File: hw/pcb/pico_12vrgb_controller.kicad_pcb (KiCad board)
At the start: 2 copper layers, 101 x 31.8 mm, 20 parts, among them J1 Conn_01x04_RGB, J2 Conn_01x04_RGB, J3 Conn_01x04_RGB, J4 Conn_01x04_RGB, J5 Sata_15pin_Power, Q1 DMG2302U, Q10 DMG2302U, Q11 DMG2302U, Q12 DMG2302U, Q2 DMG2302U, Q3 DMG2302U, Q4 DMG2302U, Q5 DMG2302U, Q6 DMG2302U, Q7 DMG2302U, Q8 DMG2302U, Q9 DMG2302U, U1 Raspberry_Pi_Pico, U2 LM4040C30FTA

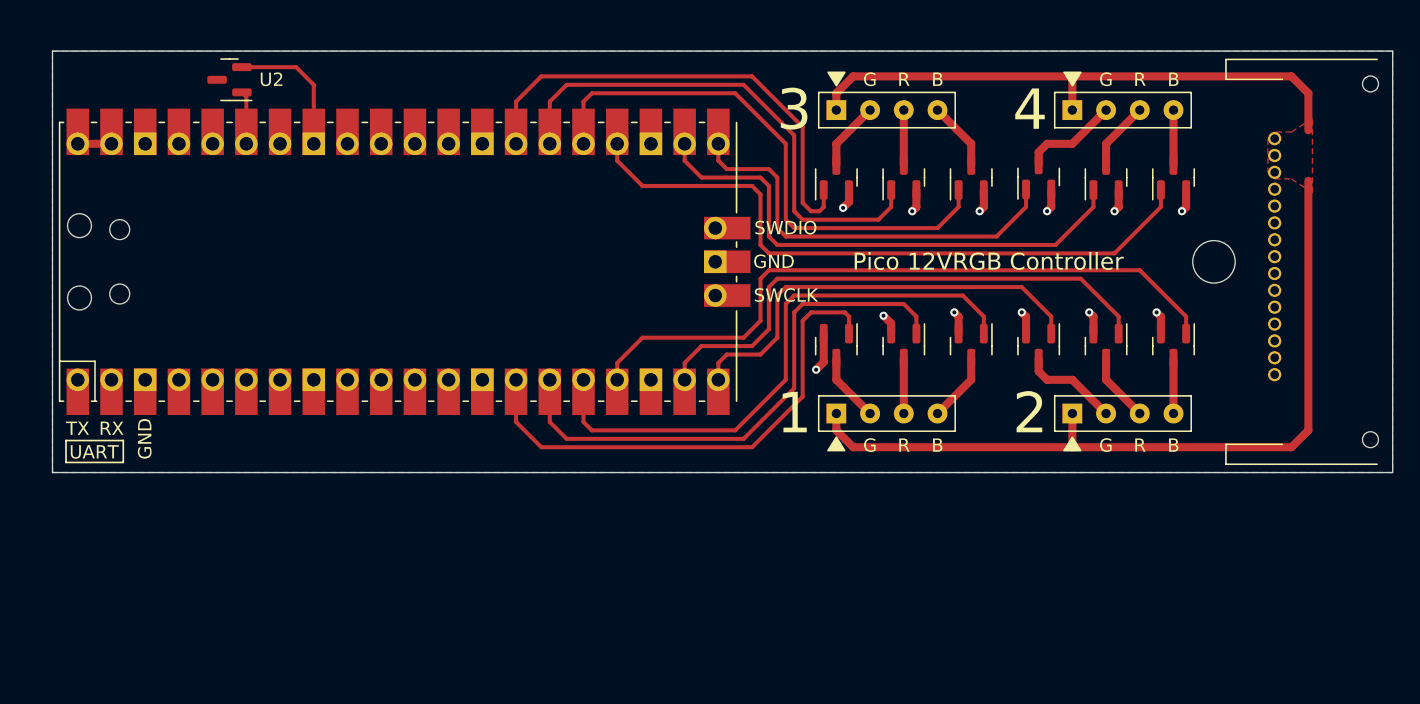
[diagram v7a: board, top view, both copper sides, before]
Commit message: Add missing silkscreen markings
Change debug label, add transistor markings, add version number.
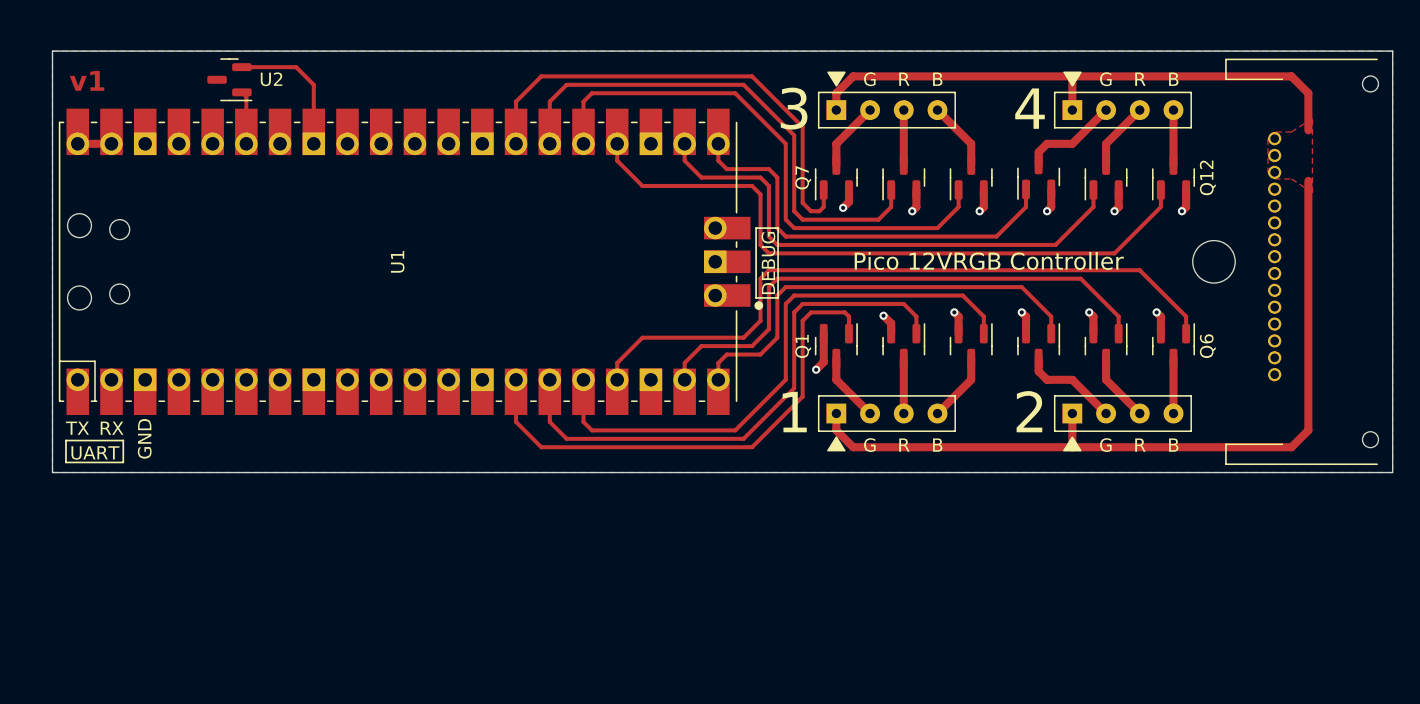
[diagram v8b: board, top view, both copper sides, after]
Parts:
- renumbered Q3 to Q1, Q12 to Q10, Q10 to Q12, Q1 to Q3, Q6 to Q4, Q4 to Q6, Q9 to Q7, Q7 to Q9
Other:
- board text added: "DEBUG"
- board text added: "v1"
- board text removed: "SWCLK"
- board text removed: "SWDIO"
